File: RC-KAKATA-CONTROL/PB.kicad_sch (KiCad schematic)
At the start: 20 parts, among them SW1 TS-1088-AR02016, SW2 TS-1088-AR02016, SW3 TS-1088-AR02016, SW4 TS-1088-AR02016, SW6 TS-1088-AR02016

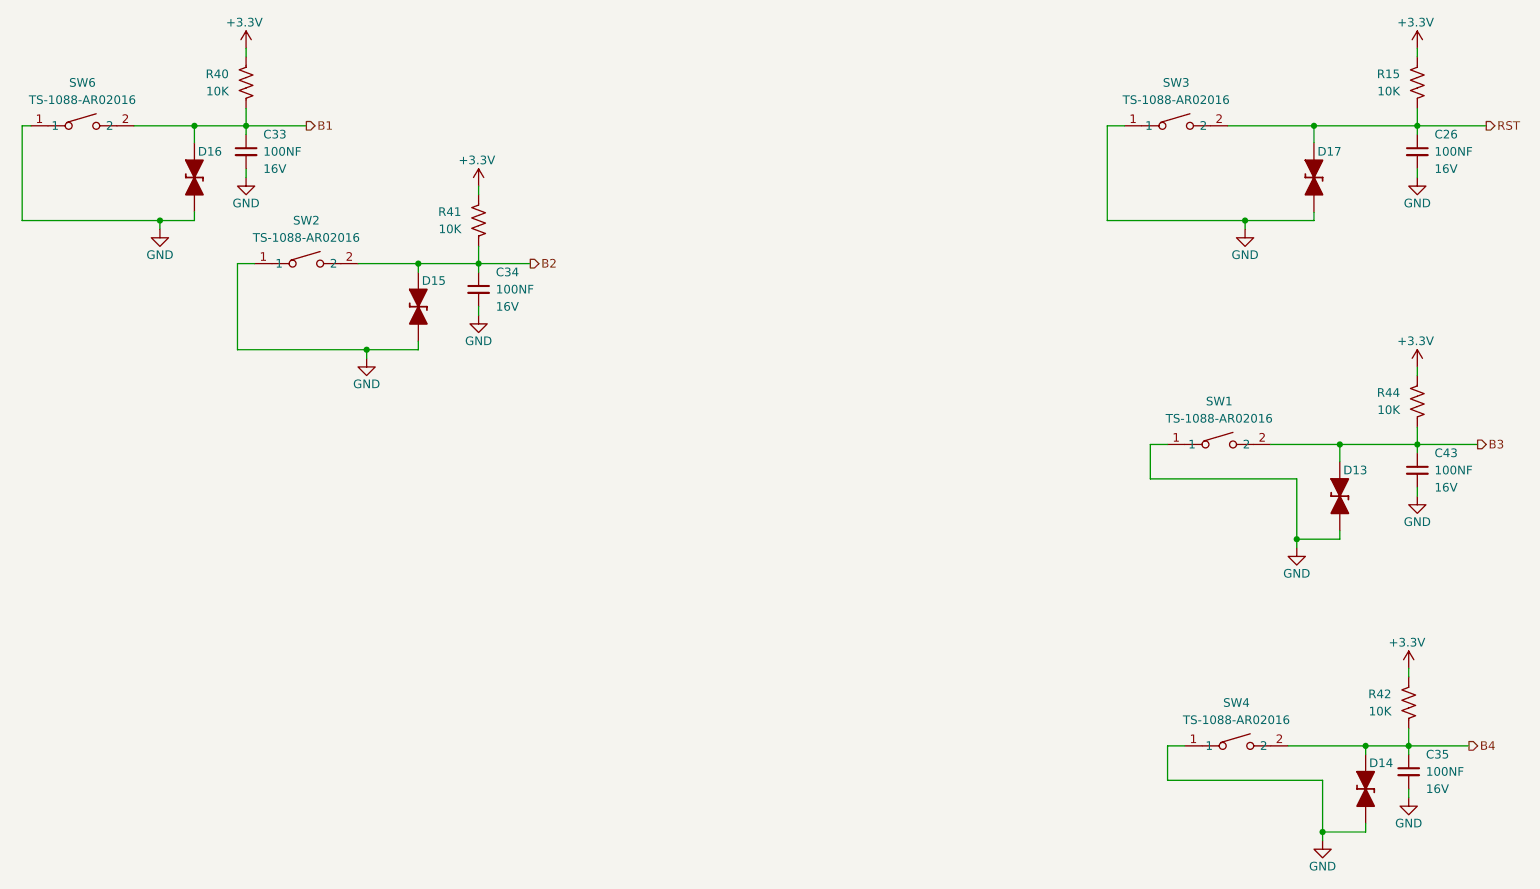
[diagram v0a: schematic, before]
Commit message: Agregadas conexiones de analogicos Agregadas las conexiones de i2c Agregadas las conexiones de Uart Cambiados algunos detalles de tvs resistencias y cap Recolocados los componenetes de power supply Cambiados los diodos de entrada de la bateria por unos de 5A Cambios menores y mejorada la documentacion Agregada informacion en la serigrafia del PCB
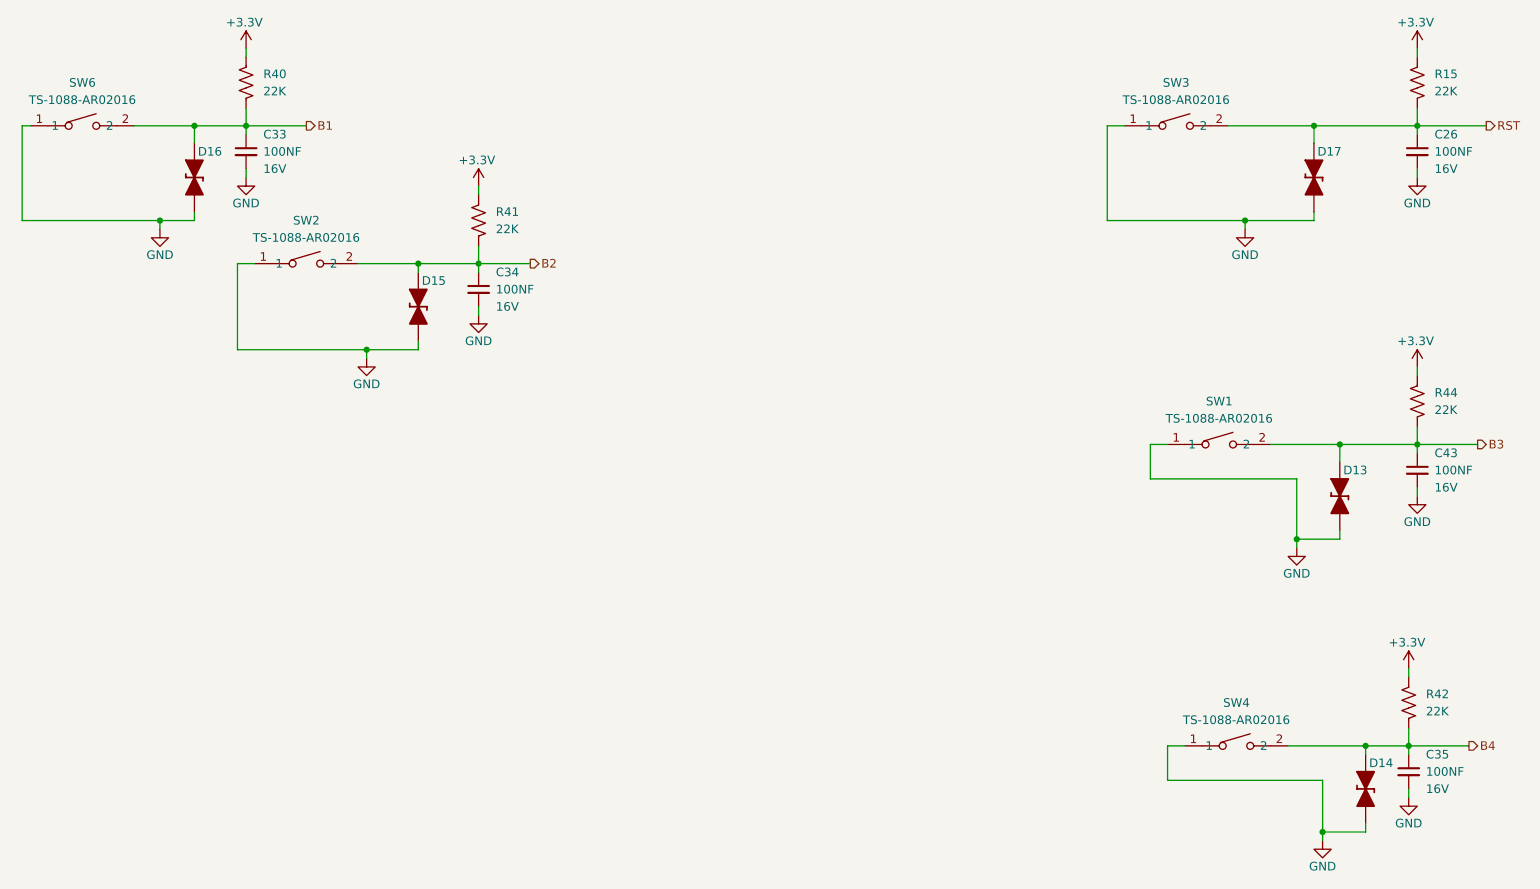
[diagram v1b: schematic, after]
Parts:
- R15, R40, R41, R42, R44: value 10K -> 22K
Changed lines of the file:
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@@
 		(fields_autoplaced yes)
 		(property "Reference" "R42"
-			(at 232.41 133.3499 0)
-			(effects
-				(font
-					(size 1.27 1.27)
-				)
-				(justify left)
-			)
-		)
-		(property "Value" "10K"
-			(at 232.41 135.8899 0)
-			(effects
-				(font
-					(size 1.27 1.27)
-				)
-				(justify left)
+			(at 237.49 133.3499 0)
+			(effects
+				(font
+					(size 1.27 1.27)
+				)
+				(justify right)
+			)
+		)
+		(property "Value" "22K"
+			(at 237.49 135.8899 0)
+			(effects
+				(font
+					(size 1.27 1.27)
+				)
+				(justify right)
 			)
 		)
@@
 		(fields_autoplaced yes)
 		(property "Reference" "R15"
-			(at 233.68 41.9099 0)
-			(effects
-				(font
-					(size 1.27 1.27)
-				)
-				(justify left)
-			)
-		)
-		(property "Value" "10K"
-			(at 233.68 44.4499 0)
-			(effects
-				(font
-					(size 1.27 1.27)
-				)
-				(justify left)
+			(at 238.76 41.9099 0)
+			(effects
+				(font
+					(size 1.27 1.27)
+				)
+				(justify right)
+			)
+		)
+		(property "Value" "22K"
+			(at 238.76 44.4499 0)
+			(effects
+				(font
+					(size 1.27 1.27)
+				)
+				(justify right)
 			)
 		)
@@
 		(fields_autoplaced yes)
 		(property "Reference" "R41"
-			(at 95.25 62.2299 0)
-			(effects
-				(font
-					(size 1.27 1.27)
-				)
-				(justify left)
-			)
-		)
-		(property "Value" "10K"
-			(at 95.25 64.7699 0)
-			(effects
-				(font
-					(size 1.27 1.27)
-				)
-				(justify left)
+			(at 100.33 62.2299 0)
+			(effects
+				(font
+					(size 1.27 1.27)
+				)
+				(justify right)
+			)
+		)
+		(property "Value" "22K"
+			(at 100.33 64.7699 0)
+			(effects
+				(font
+					(size 1.27 1.27)
+				)
+				(justify right)
 			)
 		)
@@
 		(fields_autoplaced yes)
 		(property "Reference" "R44"
-			(at 233.68 88.8999 0)
-			(effects
-				(font
-					(size 1.27 1.27)
-				)
-				(justify left)
-			)
-		)
-		(property "Value" "10K"
-			(at 233.68 91.4399 0)
-			(effects
-				(font
-					(size 1.27 1.27)
-				)
-				(justify left)
+			(at 238.76 88.8999 0)
+			(effects
+				(font
+					(size 1.27 1.27)
+				)
+				(justify right)
+			)
+		)
+		(property "Value" "22K"
+			(at 238.76 91.4399 0)
+			(effects
+				(font
+					(size 1.27 1.27)
+				)
+				(justify right)
 			)
 		)
@@
 		(fields_autoplaced yes)
 		(property "Reference" "R40"
-			(at 60.96 41.9099 0)
-			(effects
-				(font
-					(size 1.27 1.27)
-				)
-				(justify left)
-			)
-		)
-		(property "Value" "10K"
-			(at 60.96 44.4499 0)
-			(effects
-				(font
-					(size 1.27 1.27)
-				)
-				(justify left)
-			)
-		)
+			(at 66.04 41.9099 0)
+			(effects
+				(font
+					(size 1.27 1.27)
+				)
+				(justify right)
+			)
+		)
+		(property "Value" "22K"
+			(at 66.04 44.4499 0)
+			(effects
+				(font
+					(size 1.27 1.27)
+				)
+				(justify right)
+			)
+		)
